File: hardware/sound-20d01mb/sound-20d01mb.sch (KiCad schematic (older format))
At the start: 10 parts

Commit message: Updated mounting holes
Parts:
- removed H? (x4): MountingHole, MountingHole:MountingHole_3.2mm_M3, symbol Mechanical:MountingHole
- added H? (x4): MountingHole_Pad, MountingHole:MountingHole_3.2mm_M3_Pad_Via, symbol Mechanical:MountingHole_Pad
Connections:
- wire segments 40 -> 44
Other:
- note added: "External 5V\n(digital)"
- note added: "Supply voltage range:\n12V to 30V (analog)"
- note removed: "External 5V (digital)"
- note removed: "Supply voltage range: 12V to 30V (analog)"
- moved on the sheet: J?
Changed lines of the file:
@@
 $EndSheet
-$Comp
-L Mechanical:MountingHole H?
-U 1 1 60DF6F4D
-P 8100 6350
-F 0 "H?" H 8200 6396 50  0000 L CNN
-F 1 "MountingHole" H 8200 6305 50  0000 L CNN
-F 2 "MountingHole:MountingHole_3.2mm_M3" H 8100 6350 50  0001 C CNN
-F 3 "~" H 8100 6350 50  0001 C CNN
-	1    8100 6350
-	1    0    0    -1
-$EndComp
-$Comp
-L Mechanical:MountingHole H?
-U 1 1 60DF9883
-P 8900 6350
-F 0 "H?" H 9000 6396 50  0000 L CNN
-F 1 "MountingHole" H 9000 6305 50  0000 L CNN
-F 2 "MountingHole:MountingHole_3.2mm_M3" H 8900 6350 50  0001 C CNN
-F 3 "~" H 8900 6350 50  0001 C CNN
-	1    8900 6350
-	1    0    0    -1
-$EndComp
-$Comp
-L Mechanical:MountingHole H?
-U 1 1 60DF98C1
-P 9700 6350
-F 0 "H?" H 9800 6396 50  0000 L CNN
-F 1 "MountingHole" H 9800 6305 50  0000 L CNN
-F 2 "MountingHole:MountingHole_3.2mm_M3" H 9700 6350 50  0001 C CNN
-F 3 "~" H 9700 6350 50  0001 C CNN
-	1    9700 6350
-	1    0    0    -1
-$EndComp
-$Comp
-L Mechanical:MountingHole H?
-U 1 1 60DF9924
-P 10500 6350
-F 0 "H?" H 10600 6396 50  0000 L CNN
-F 1 "MountingHole" H 10600 6305 50  0000 L CNN
-F 2 "MountingHole:MountingHole_3.2mm_M3" H 10500 6350 50  0001 C CNN
-F 3 "~" H 10500 6350 50  0001 C CNN
-	1    10500 6350
-	1    0    0    -1
-$EndComp
 $Comp
 L Connector:USB_B J?
@@
 L Connector_Generic:Conn_01x02 J?
 U 1 1 60E0FD2A
-P 6750 3400
-F 0 "J?" H 6830 3392 50  0000 L CNN
-F 1 "Conn_01x02" H 6830 3301 50  0000 L CNN
-F 2 "Connector_JST:JST_VH_B2P-VH_1x02_P3.96mm_Vertical" H 6750 3400 50  0001 C CNN
-F 3 "~" H 6750 3400 50  0001 C CNN
-	1    6750 3400
+P 8600 5350
+F 0 "J?" H 8680 5342 50  0000 L CNN
+F 1 "Conn_01x02" H 8680 5251 50  0000 L CNN
+F 2 "Connector_JST:JST_VH_B2P-VH_1x02_P3.96mm_Vertical" H 8600 5350 50  0001 C CNN
+F 3 "~" H 8600 5350 50  0001 C CNN
+	1    8600 5350
 	1    0    0    -1
 $EndComp
@@
 L power:GNDA #PWR?
 U 1 1 60E0FF3C
-P 6450 3600
-F 0 "#PWR?" H 6450 3350 50  0001 C CNN
-F 1 "GNDA" H 6455 3427 50  0000 C CNN
-F 2 "" H 6450 3600 50  0001 C CNN
-F 3 "" H 6450 3600 50  0001 C CNN
-	1    6450 3600
-	1    0    0    -1
-$EndComp
-Wire Wire Line
-	6550 3500 6450 3500
-Wire Wire Line
-	6450 3500 6450 3600
+P 8300 5550
+F 0 "#PWR?" H 8300 5300 50  0001 C CNN
+F 1 "GNDA" H 8305 5377 50  0000 C CNN
+F 2 "" H 8300 5550 50  0001 C CNN
+F 3 "" H 8300 5550 50  0001 C CNN
+	1    8300 5550
+	1    0    0    -1
+$EndComp
+Wire Wire Line
+	8400 5450 8300 5450
+Wire Wire Line
+	8300 5450 8300 5550
 $Comp
 L power:VCC #PWR?
 U 1 1 60E100F5
-P 6450 3300
-F 0 "#PWR?" H 6450 3150 50  0001 C CNN
-F 1 "VCC" H 6467 3473 50  0000 C CNN
-F 2 "" H 6450 3300 50  0001 C CNN
-F 3 "" H 6450 3300 50  0001 C CNN
-	1    6450 3300
-	1    0    0    -1
-$EndComp
-Wire Wire Line
-	6550 3400 6450 3400
-Wire Wire Line
-	6450 3400 6450 3300
-Text Notes 6700 3300 0    50   ~ 0
-Supply voltage range: 12V to 30V (analog)
+P 8300 5250
+F 0 "#PWR?" H 8300 5100 50  0001 C CNN
+F 1 "VCC" H 8317 5423 50  0000 C CNN
+F 2 "" H 8300 5250 50  0001 C CNN
+F 3 "" H 8300 5250 50  0001 C CNN
+	1    8300 5250
+	1    0    0    -1
+$EndComp
+Wire Wire Line
+	8400 5350 8300 5350
+Wire Wire Line
+	8300 5350 8300 5250
+Text Notes 8550 5250 0    50   ~ 0
+Supply voltage range:\n12V to 30V (analog)
 $Comp
 L power:VBUS #PWR?
@@
 L Connector_Generic:Conn_01x02 J?
 U 1 1 60EA1B68
-P 4200 4600
-F 0 "J?" H 4280 4592 50  0000 L CNN
-F 1 "Conn_01x02" H 4280 4501 50  0000 L CNN
-F 2 "Connector_JST:JST_XH_B02B-XH-A_1x02_P2.50mm_Vertical" H 4200 4600 50  0001 C CNN
-F 3 "~" H 4200 4600 50  0001 C CNN
-	1    4200 4600
+P 7600 5350
+F 0 "J?" H 7680 5342 50  0000 L CNN
+F 1 "Conn_01x02" H 7680 5251 50  0000 L CNN
+F 2 "Connector_JST:JST_XH_B02B-XH-A_1x02_P2.50mm_Vertical" H 7600 5350 50  0001 C CNN
+F 3 "~" H 7600 5350 50  0001 C CNN
+	1    7600 5350
 	1    0    0    -1
 $EndComp
@@
 L power:GNDD #PWR?
 U 1 1 60EA1BF4
-P 3900 4800
-F 0 "#PWR?" H 3900 4550 50  0001 C CNN
-F 1 "GNDD" H 3904 4645 50  0000 C CNN
-F 2 "" H 3900 4800 50  0001 C CNN
-F 3 "" H 3900 4800 50  0001 C CNN
-	1    3900 4800
-	1    0    0    -1
-$EndComp
-Wire Wire Line
-	4000 4700 3900 4700
-Wire Wire Line
-	3900 4700 3900 4800
-Text Notes 4150 4500 0    50   ~ 0
-External 5V (digital)
+P 7300 5550
+F 0 "#PWR?" H 7300 5300 50  0001 C CNN
+F 1 "GNDD" H 7304 5395 50  0000 C CNN
+F 2 "" H 7300 5550 50  0001 C CNN
+F 3 "" H 7300 5550 50  0001 C CNN
+	1    7300 5550
+	1    0    0    -1
+$EndComp
+Wire Wire Line
+	7400 5450 7300 5450
+Wire Wire Line
+	7300 5450 7300 5550
+Text Notes 7550 5250 0    50   ~ 0
+External 5V\n(digital)
 Wire Wire Line
 	3650 2350 5050 2350
@@
 L power:+5V #PWR?
 U 1 1 6153EEDC
-P 3900 4500
-F 0 "#PWR?" H 3900 4350 50  0001 C CNN
-F 1 "+5V" H 3915 4673 50  0000 C CNN
-F 2 "" H 3900 4500 50  0001 C CNN
-F 3 "" H 3900 4500 50  0001 C CNN
-	1    3900 4500
-	1    0    0    -1
-$EndComp
-Wire Wire Line
-	4000 4600 3900 4600
-Wire Wire Line
-	3900 4600 3900 4500
+P 7300 5250
+F 0 "#PWR?" H 7300 5100 50  0001 C CNN
+F 1 "+5V" H 7315 5423 50  0000 C CNN
+F 2 "" H 7300 5250 50  0001 C CNN
+F 3 "" H 7300 5250 50  0001 C CNN
+	1    7300 5250
+	1    0    0    -1
+$EndComp
+Wire Wire Line
+	7400 5350 7300 5350
+Wire Wire Line
+	7300 5350 7300 5250
 Wire Wire Line
 	1950 1600 2050 1600
 Wire Wire Line
 	2050 1600 2050 1500
+$Comp
+L Mechanical:MountingHole_Pad H?
+U 1 1 615D7541
+P 7300 6000
+F 0 "H?" H 7400 6051 50  0000 L CNN
+F 1 "MountingHole_Pad" H 7400 5960 50  0000 L CNN
+F 2 "MountingHole:MountingHole_3.2mm_M3_Pad_Via" H 7300 6000 50  0001 C CNN
+F 3 "~" H 7300 6000 50  0001 C CNN
+	1    7300 6000
+	1    0    0    -1
+$EndComp
+Wire Wire Line
+	7300 6100 7300 6200
+$Comp
+L Mechanical:MountingHole_Pad H?
+U 1 1 615D7F85
+P 8300 6000
+F 0 "H?" H 8400 6051 50  0000 L CNN
+F 1 "MountingHole_Pad" H 8400 5960 50  0000 L CNN
+F 2 "MountingHole:MountingHole_3.2mm_M3_Pad_Via" H 8300 6000 50  0001 C CNN
+F 3 "~" H 8300 6000 50  0001 C CNN
+	1    8300 6000
+	1    0    0    -1
+$EndComp
+Wire Wire Line
+	8300 6100 8300 6200
+$Comp
+L Mechanical:MountingHole_Pad H?
+U 1 1 615DA23B
+P 9300 6000
+F 0 "H?" H 9400 6051 50  0000 L CNN
+F 1 "MountingHole_Pad" H 9400 5960 50  0000 L CNN
+F 2 "MountingHole:MountingHole_3.2mm_M3_Pad_Via" H 9300 6000 50  0001 C CNN
+F 3 "~" H 9300 6000 50  0001 C CNN
+	1    9300 6000
+	1    0    0    -1
+$EndComp
+$Comp
+L power:GNDA #PWR?
+U 1 1 615DA241
+P 7300 6200
+F 0 "#PWR?" H 7300 5950 50  0001 C CNN
+F 1 "GNDA" H 7305 6027 50  0000 C CNN
+F 2 "" H 7300 6200 50  0001 C CNN
+F 3 "" H 7300 6200 50  0001 C CNN
+	1    7300 6200
+	1    0    0    -1
+$EndComp
+Wire Wire Line
+	9300 6100 9300 6200
+$Comp
+L Mechanical:MountingHole_Pad H?
+U 1 1 615DA248
+P 10300 6000
+F 0 "H?" H 10400 6051 50  0000 L CNN
+F 1 "MountingHole_Pad" H 10400 5960 50  0000 L CNN
+F 2 "MountingHole:MountingHole_3.2mm_M3_Pad_Via" H 10300 6000 50  0001 C CNN
+F 3 "~" H 10300 6000 50  0001 C CNN
+	1    10300 6000
+	1    0    0    -1
+$EndComp
+Wire Wire Line
+	10300 6100 10300 6200
+$Comp
+L power:GNDA #PWR?
+U 1 1 615EC7C2
+P 8300 6200
+F 0 "#PWR?" H 8300 5950 50  0001 C CNN
+F 1 "GNDA" H 8305 6027 50  0000 C CNN
+F 2 "" H 8300 6200 50  0001 C CNN
+F 3 "" H 8300 6200 50  0001 C CNN
+	1    8300 6200
+	1    0    0    -1
+$EndComp
+$Comp
+L power:GNDA #PWR?
+U 1 1 615EC7EB
+P 9300 6200
+F 0 "#PWR?" H 9300 5950 50  0001 C CNN
+F 1 "GNDA" H 9305 6027 50  0000 C CNN
+F 2 "" H 9300 6200 50  0001 C CNN
+F 3 "" H 9300 6200 50  0001 C CNN
+	1    9300 6200
+	1    0    0    -1
+$EndComp
+$Comp
+L power:GNDA #PWR?
+U 1 1 615EC814
+P 10300 6200
+F 0 "#PWR?" H 10300 5950 50  0001 C CNN
+F 1 "GNDA" H 10305 6027 50  0000 C CNN
+F 2 "" H 10300 6200 50  0001 C CNN
+F 3 "" H 10300 6200 50  0001 C CNN
+	1    10300 6200
+	1    0    0    -1
+$EndComp
 $EndSCHEMATC

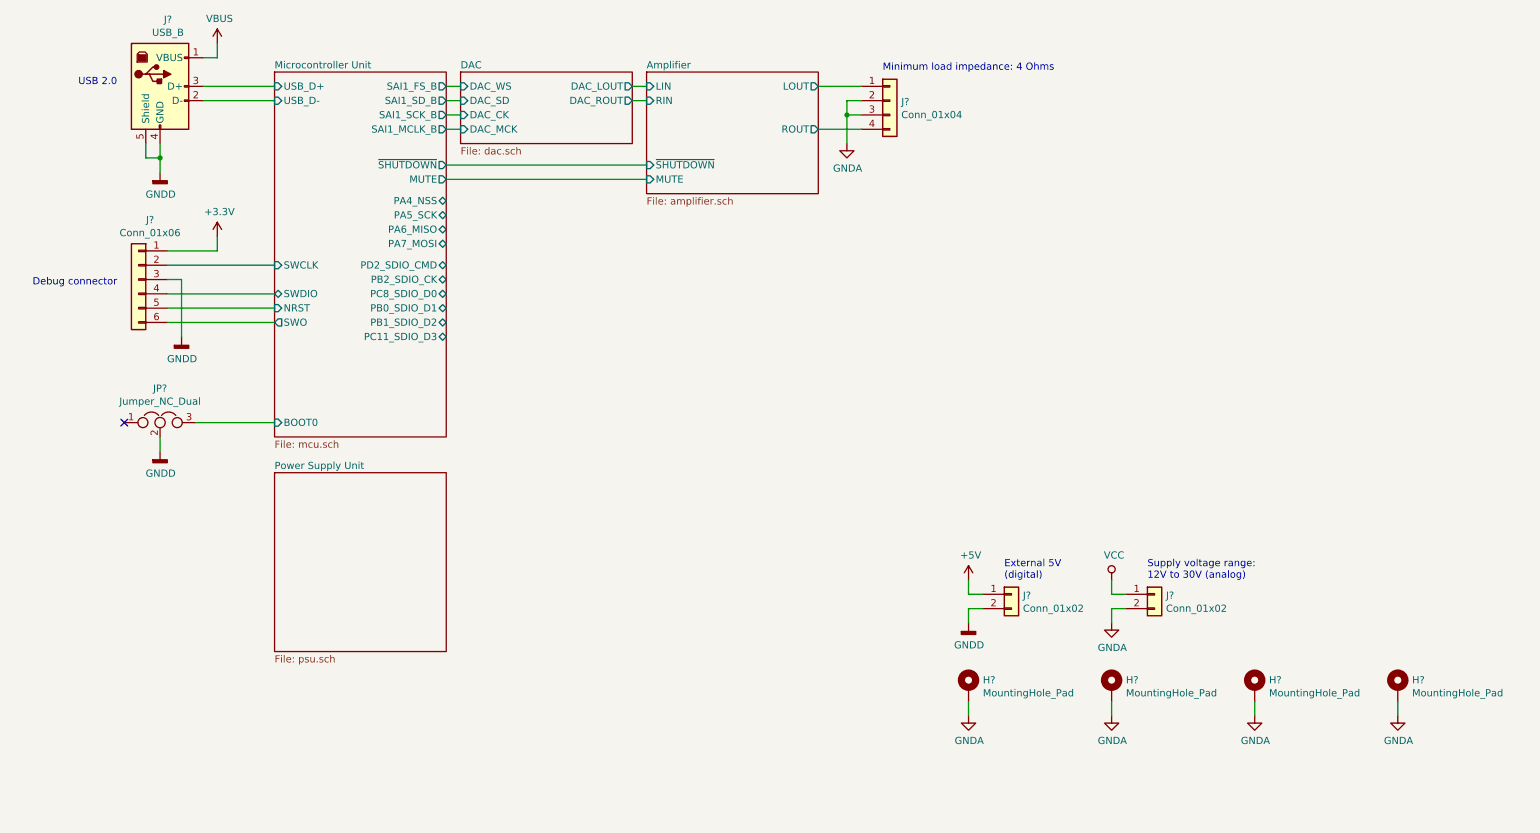
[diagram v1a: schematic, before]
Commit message: Added GPIO for MCU
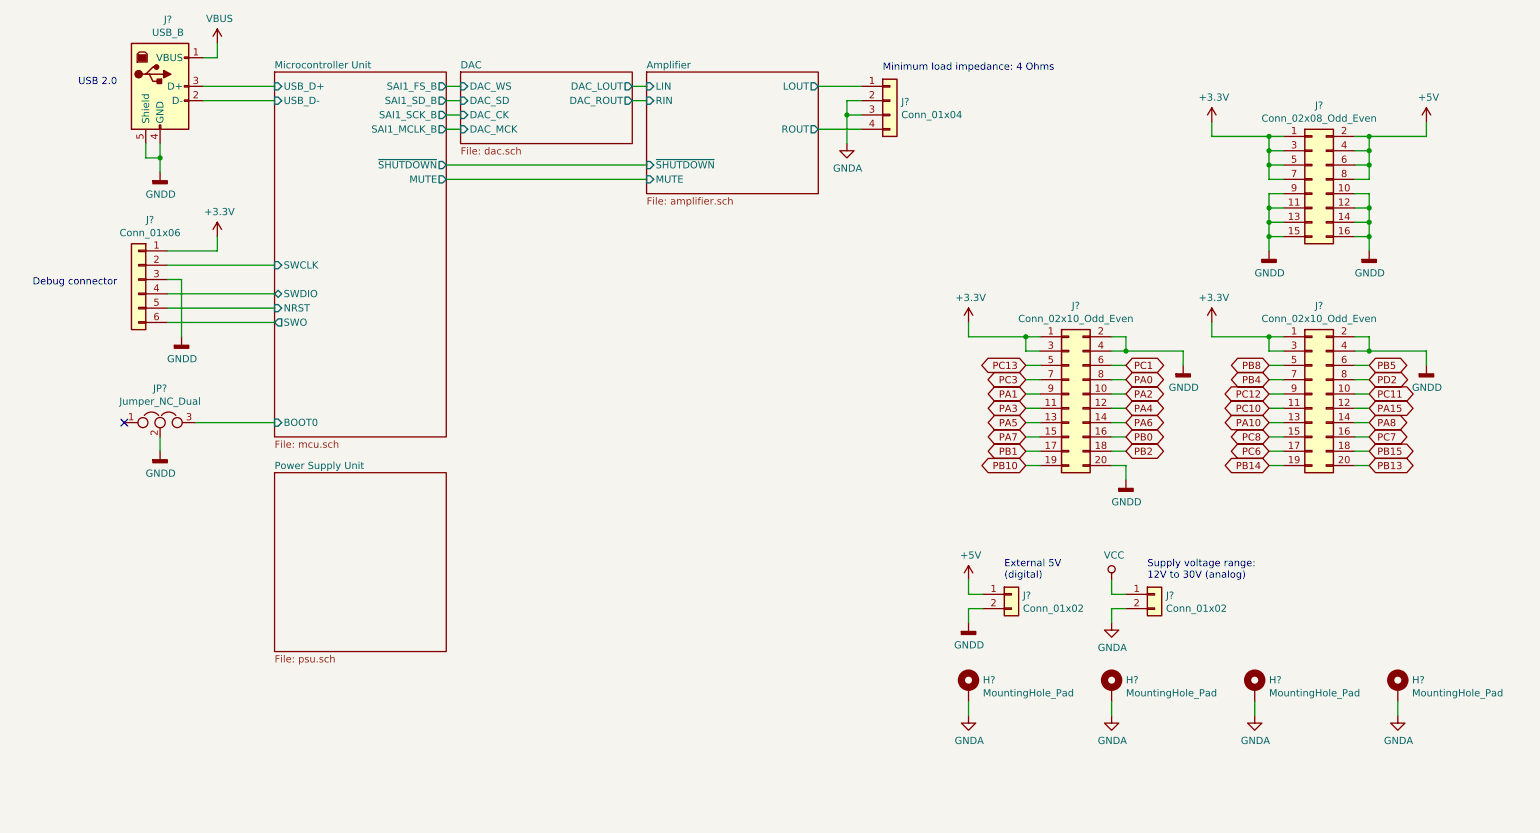
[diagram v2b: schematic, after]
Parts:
- added J? (x2): Conn_02x10_Odd_Even, Connector_PinHeader_2.54mm:PinHeader_2x10_P2.54mm_Vertical, symbol Connector_Generic:Conn_02x10_Odd_Even
- added J?: Conn_02x08_Odd_Even, Connector_PinHeader_2.54mm:PinHeader_2x08_P2.54mm_Vertical, symbol Connector_Generic:Conn_02x08_Odd_Even
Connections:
- net +3V3: now also J?.1 (Pin_1), J?.1 (Pin_1), J?.1 (Pin_1), J?.3 (Pin_3), J?.3 (Pin_3), J?.3 (Pin_3), J?.5 (Pin_5), J?.7 (Pin_7)
- net +5V: now also J?.2 (Pin_2), J?.4 (Pin_4), J?.6 (Pin_6), J?.8 (Pin_8)
- net GNDD: now also J?.10 (Pin_10), J?.11 (Pin_11), J?.12 (Pin_12), J?.13 (Pin_13), J?.14 (Pin_14), J?.15 (Pin_15), J?.16 (Pin_16), J?.2 (Pin_2), J?.2 (Pin_2), J?.20 (Pin_20), J?.4 (Pin_4), J?.4 (Pin_4), J?.9 (Pin_9)
- new net PA0: J?.8 (Pin_8)
- new net PA1: J?.9 (Pin_9)
- new net PA10: J?.13 (Pin_13)
- new net PA15: J?.12 (Pin_12)
- new net PA2: J?.10 (Pin_10)
- new net PA3: J?.11 (Pin_11)
- new net PA4: J?.12 (Pin_12)
- new net PA5: J?.13 (Pin_13)
- new net PA6: J?.14 (Pin_14)
- new net PA7: J?.15 (Pin_15)
- new net PA8: J?.14 (Pin_14)
- new net PB0: J?.16 (Pin_16)
- new net PB1: J?.17 (Pin_17)
- new net PB10: J?.19 (Pin_19)
- new net PB13: J?.20 (Pin_20)
- new net PB14: J?.19 (Pin_19)
- new net PB15: J?.18 (Pin_18)
- new net PB2: J?.18 (Pin_18)
- new net PB4: J?.7 (Pin_7)
- new net PB5: J?.6 (Pin_6)
- new net PB8: J?.5 (Pin_5)
- new net PC1: J?.6 (Pin_6)
- new net PC10: J?.11 (Pin_11)
- new net PC11: J?.10 (Pin_10)
- new net PC12: J?.9 (Pin_9)
- new net PC13: J?.5 (Pin_5)
- new net PC3: J?.7 (Pin_7)
- new net PC6: J?.17 (Pin_17)
- new net PC7: J?.16 (Pin_16)
- new net PC8: J?.15 (Pin_15)
- new net PD2: J?.8 (Pin_8)

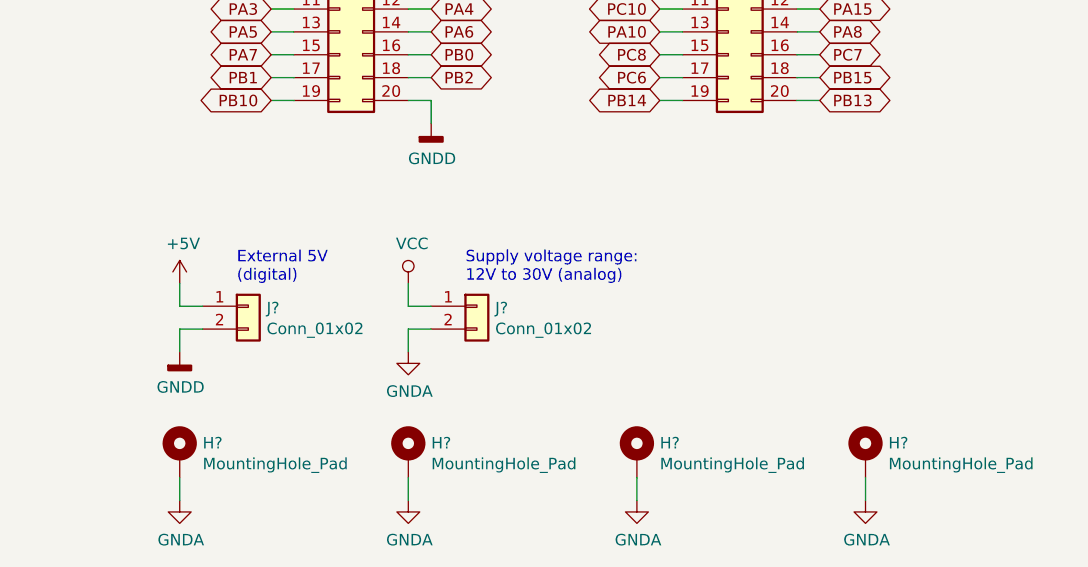
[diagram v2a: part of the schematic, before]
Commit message: Added RTC-BAT
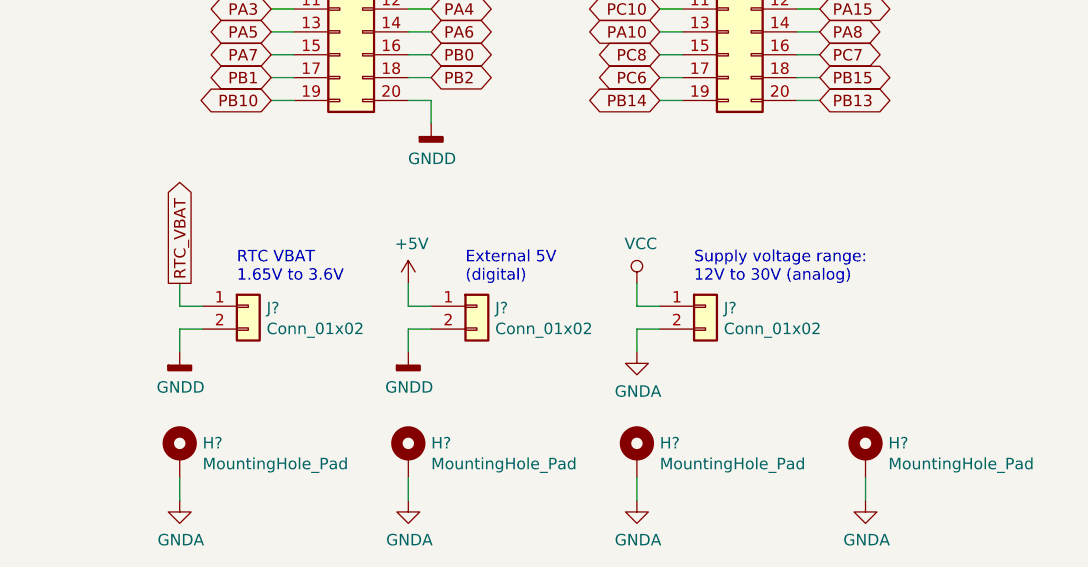
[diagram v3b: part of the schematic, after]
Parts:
- added J?: Conn_01x02, Connector_JST:JST_XH_B02B-XH-A_1x02_P2.50mm_Vertical, symbol Connector_Generic:Conn_01x02
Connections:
- net GNDD: now also J?.2 (Pin_2)
- new net RTC_VBAT: J?.1 (Pin_1)
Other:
- note added: "RTC VBAT\n1.65V to 3.6V"
- moved on the sheet: J?
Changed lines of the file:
@@
 L Connector_Generic:Conn_01x02 J?
 U 1 1 60E0FD2A
-P 8600 5350
-F 0 "J?" H 8680 5342 50  0000 L CNN
-F 1 "Conn_01x02" H 8680 5251 50  0000 L CNN
-F 2 "Connector_JST:JST_VH_B2P-VH_1x02_P3.96mm_Vertical" H 8600 5350 50  0001 C CNN
-F 3 "~" H 8600 5350 50  0001 C CNN
-	1    8600 5350
+P 9600 5350
+F 0 "J?" H 9680 5342 50  0000 L CNN
+F 1 "Conn_01x02" H 9680 5251 50  0000 L CNN
+F 2 "Connector_JST:JST_VH_B2P-VH_1x02_P3.96mm_Vertical" H 9600 5350 50  0001 C CNN
+F 3 "~" H 9600 5350 50  0001 C CNN
+	1    9600 5350
 	1    0    0    -1
 $EndComp
@@
 L power:GNDA #PWR?
 U 1 1 60E0FF3C
-P 8300 5550
-F 0 "#PWR?" H 8300 5300 50  0001 C CNN
-F 1 "GNDA" H 8305 5377 50  0000 C CNN
-F 2 "" H 8300 5550 50  0001 C CNN
-F 3 "" H 8300 5550 50  0001 C CNN
-	1    8300 5550
-	1    0    0    -1
-$EndComp
-Wire Wire Line
-	8400 5450 8300 5450
-Wire Wire Line
-	8300 5450 8300 5550
+P 9300 5550
+F 0 "#PWR?" H 9300 5300 50  0001 C CNN
+F 1 "GNDA" H 9305 5377 50  0000 C CNN
+F 2 "" H 9300 5550 50  0001 C CNN
+F 3 "" H 9300 5550 50  0001 C CNN
+	1    9300 5550
+	1    0    0    -1
+$EndComp
+Wire Wire Line
+	9400 5450 9300 5450
+Wire Wire Line
+	9300 5450 9300 5550
 $Comp
 L power:VCC #PWR?
 U 1 1 60E100F5
-P 8300 5250
-F 0 "#PWR?" H 8300 5100 50  0001 C CNN
-F 1 "VCC" H 8317 5423 50  0000 C CNN
-F 2 "" H 8300 5250 50  0001 C CNN
-F 3 "" H 8300 5250 50  0001 C CNN
-	1    8300 5250
-	1    0    0    -1
-$EndComp
-Wire Wire Line
-	8400 5350 8300 5350
-Wire Wire Line
-	8300 5350 8300 5250
-Text Notes 8550 5250 0    50   ~ 0
+P 9300 5250
+F 0 "#PWR?" H 9300 5100 50  0001 C CNN
+F 1 "VCC" H 9317 5423 50  0000 C CNN
+F 2 "" H 9300 5250 50  0001 C CNN
+F 3 "" H 9300 5250 50  0001 C CNN
+	1    9300 5250
+	1    0    0    -1
+$EndComp
+Wire Wire Line
+	9400 5350 9300 5350
+Wire Wire Line
+	9300 5350 9300 5250
+Text Notes 9550 5250 0    50   ~ 0
 Supply voltage range:\n12V to 30V (analog)
 $Comp
@@
 L Connector_Generic:Conn_01x02 J?
 U 1 1 60EA1B68
-P 7600 5350
-F 0 "J?" H 7680 5342 50  0000 L CNN
-F 1 "Conn_01x02" H 7680 5251 50  0000 L CNN
-F 2 "Connector_JST:JST_XH_B02B-XH-A_1x02_P2.50mm_Vertical" H 7600 5350 50  0001 C CNN
-F 3 "~" H 7600 5350 50  0001 C CNN
-	1    7600 5350
+P 8600 5350
+F 0 "J?" H 8680 5342 50  0000 L CNN
+F 1 "Conn_01x02" H 8680 5251 50  0000 L CNN
+F 2 "Connector_JST:JST_XH_B02B-XH-A_1x02_P2.50mm_Vertical" H 8600 5350 50  0001 C CNN
+F 3 "~" H 8600 5350 50  0001 C CNN
+	1    8600 5350
 	1    0    0    -1
 $EndComp
@@
 L power:GNDD #PWR?
 U 1 1 60EA1BF4
-P 7300 5550
-F 0 "#PWR?" H 7300 5300 50  0001 C CNN
-F 1 "GNDD" H 7304 5395 50  0000 C CNN
-F 2 "" H 7300 5550 50  0001 C CNN
-F 3 "" H 7300 5550 50  0001 C CNN
-	1    7300 5550
-	1    0    0    -1
-$EndComp
-Wire Wire Line
-	7400 5450 7300 5450
-Wire Wire Line
-	7300 5450 7300 5550
-Text Notes 7550 5250 0    50   ~ 0
+P 8300 5550
+F 0 "#PWR?" H 8300 5300 50  0001 C CNN
+F 1 "GNDD" H 8304 5395 50  0000 C CNN
+F 2 "" H 8300 5550 50  0001 C CNN
+F 3 "" H 8300 5550 50  0001 C CNN
+	1    8300 5550
+	1    0    0    -1
+$EndComp
+Wire Wire Line
+	8400 5450 8300 5450
+Wire Wire Line
+	8300 5450 8300 5550
+Text Notes 8550 5250 0    50   ~ 0
 External 5V\n(digital)
 Wire Wire Line
@@
 L power:+5V #PWR?
 U 1 1 6153EEDC
-P 7300 5250
-F 0 "#PWR?" H 7300 5100 50  0001 C CNN
-F 1 "+5V" H 7315 5423 50  0000 C CNN
-F 2 "" H 7300 5250 50  0001 C CNN
-F 3 "" H 7300 5250 50  0001 C CNN
-	1    7300 5250
-	1    0    0    -1
-$EndComp
-Wire Wire Line
-	7400 5350 7300 5350
-Wire Wire Line
-	7300 5350 7300 5250
+P 8300 5250
+F 0 "#PWR?" H 8300 5100 50  0001 C CNN
+F 1 "+5V" H 8315 5423 50  0000 C CNN
+F 2 "" H 8300 5250 50  0001 C CNN
+F 3 "" H 8300 5250 50  0001 C CNN
+	1    8300 5250
+	1    0    0    -1
+$EndComp
+Wire Wire Line
+	8400 5350 8300 5350
+Wire Wire Line
+	8300 5350 8300 5250
 Wire Wire Line
 	1950 1600 2050 1600
@@
 Wire Wire Line
 	8400 4450 8400 4550
+$Comp
+L Connector_Generic:Conn_01x02 J?
+U 1 1 61A12F95
+P 7600 5350
+F 0 "J?" H 7680 5342 50  0000 L CNN
+F 1 "Conn_01x02" H 7680 5251 50  0000 L CNN
+F 2 "Connector_JST:JST_XH_B02B-XH-A_1x02_P2.50mm_Vertical" H 7600 5350 50  0001 C CNN
+F 3 "~" H 7600 5350 50  0001 C CNN
+	1    7600 5350
+	1    0    0    -1
+$EndComp
+$Comp
+L power:GNDD #PWR?
+U 1 1 61A12F9B
+P 7300 5550
+F 0 "#PWR?" H 7300 5300 50  0001 C CNN
+F 1 "GNDD" H 7304 5395 50  0000 C CNN
+F 2 "" H 7300 5550 50  0001 C CNN
+F 3 "" H 7300 5550 50  0001 C CNN
+	1    7300 5550
+	1    0    0    -1
+$EndComp
+Wire Wire Line
+	7400 5450 7300 5450
+Wire Wire Line
+	7300 5450 7300 5550
+Text Notes 7550 5250 0    50   ~ 0
+RTC VBAT\n1.65V to 3.6V
+Wire Wire Line
+	7400 5350 7300 5350
+Wire Wire Line
+	7300 5350 7300 5250
+Text GLabel 7300 5250 1    50   Output ~ 0
+RTC_VBAT
 $EndSCHEMATC
